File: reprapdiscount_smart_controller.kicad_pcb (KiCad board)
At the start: 2 copper layers, 150 x 55 mm, 56 parts, among them J1 USB_A, Q1 BC817, Q2 BC817, U1 74HC4050, U2 74HC4050, U3 Pico

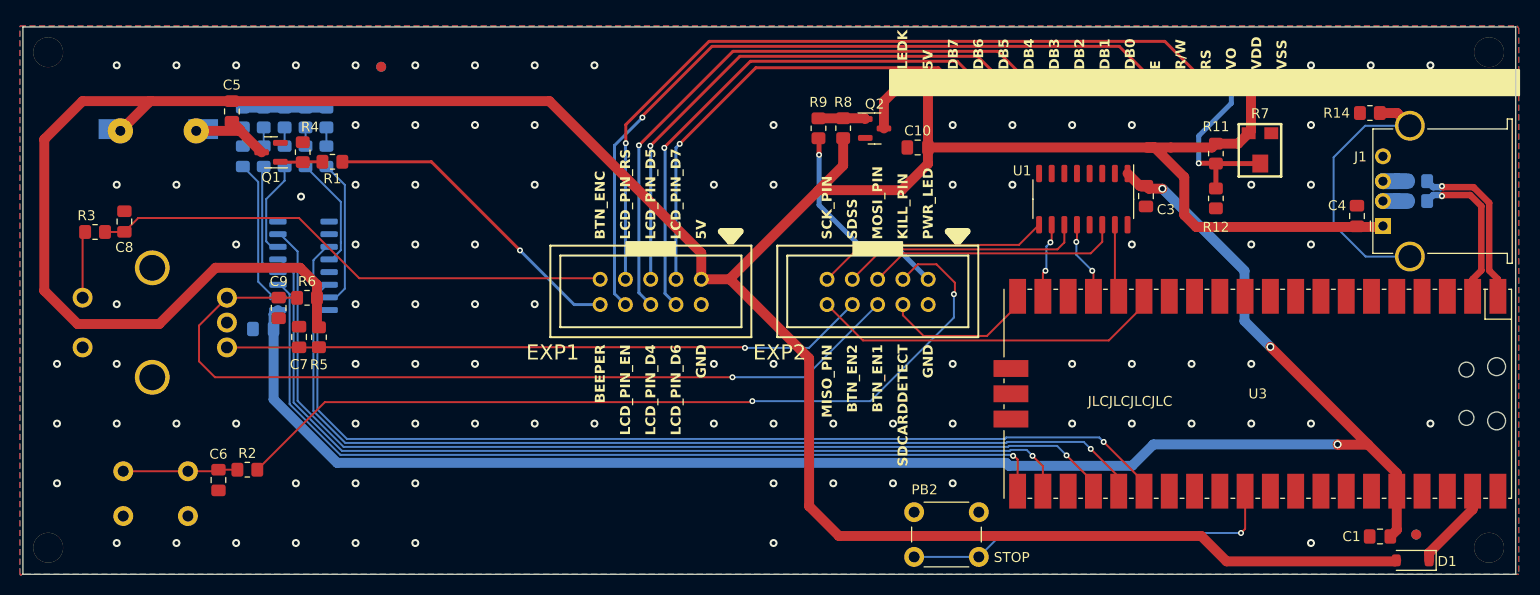
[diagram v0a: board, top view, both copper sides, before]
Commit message: feature: support adafruit rgb display
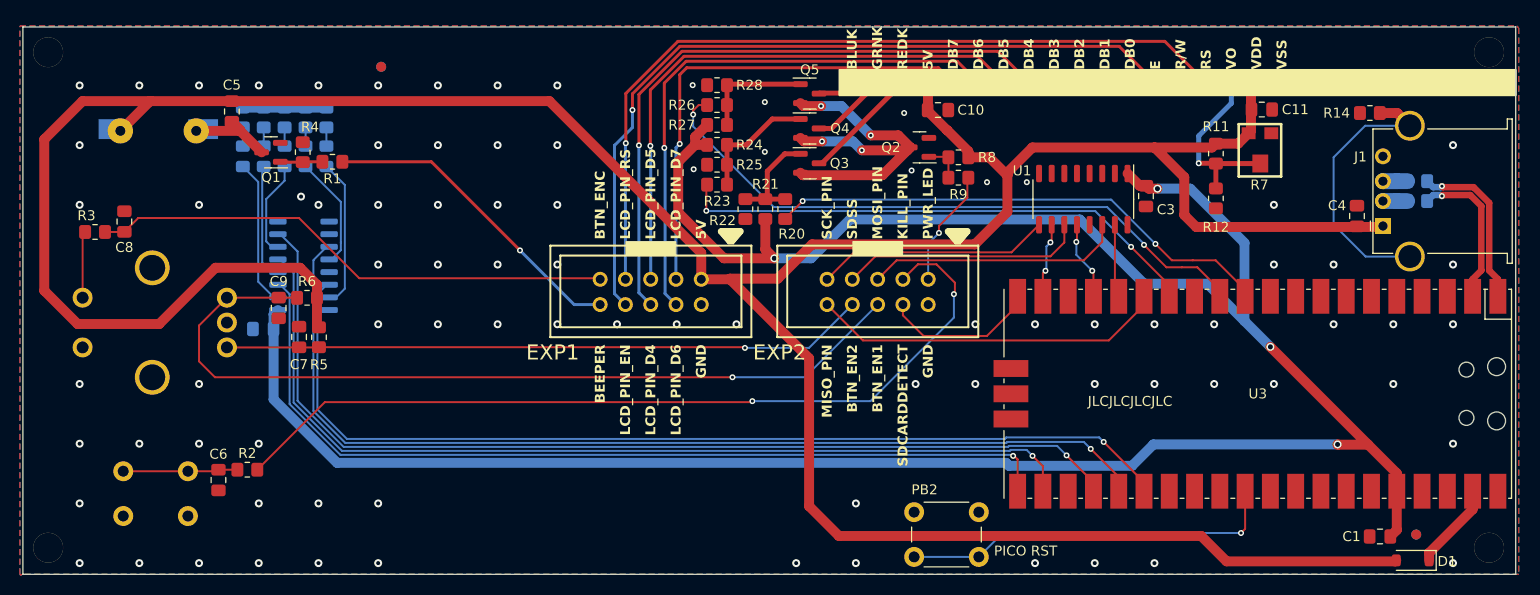
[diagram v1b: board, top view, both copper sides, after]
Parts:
- added C11: 10u, Capacitor_SMD:C_0805_2012Metric_Pad1.18x1.45mm_HandSolder, F.Cu at (198.0, 85.8)
- added Q3: DMN2005K-7, Package_TO_SOT_SMD:SOT-23, F.Cu at (152.6, 91.2)
- added Q4: DMN2005K-7, Package_TO_SOT_SMD:SOT-23, F.Cu at (152.6, 87.7)
- added Q5: DMN2005K-7, Package_TO_SOT_SMD:SOT-23, F.Cu at (152.6, 84.2)
- added R20: 0R, Resistor_SMD:R_0805_2012Metric_Pad1.20x1.40mm_HandSolder, F.Cu at (150.1, 95.8)
- added R21: 10k, Resistor_SMD:R_0805_2012Metric_Pad1.20x1.40mm_HandSolder, F.Cu at (148.1, 95.8)
- added R22: 10k, Resistor_SMD:R_0805_2012Metric_Pad1.20x1.40mm_HandSolder, F.Cu at (146.1, 95.8)
- added R23: 0R, Resistor_SMD:R_0805_2012Metric_Pad1.20x1.40mm_HandSolder, F.Cu at (143.2, 93.3)
- added R24: 10k, Resistor_SMD:R_0805_2012Metric_Pad1.20x1.40mm_HandSolder, F.Cu at (143.2, 89.3)
- added R25: 10k, Resistor_SMD:R_0805_2012Metric_Pad1.20x1.40mm_HandSolder, F.Cu at (143.2, 91.3)
- added R26: 0R, Resistor_SMD:R_0805_2012Metric_Pad1.20x1.40mm_HandSolder, F.Cu at (143.2, 85.3)
- added R27: 10k, Resistor_SMD:R_0805_2012Metric_Pad1.20x1.40mm_HandSolder, F.Cu at (143.2, 87.3)
- added R28: 10k, Resistor_SMD:R_0805_2012Metric_Pad1.20x1.40mm_HandSolder, F.Cu at (143.2, 83.3)
- LCD1: footprint reprapdiscount_smart_controller:HDR1X16 -> reprapdiscount_smart_controller:HDR1X18
- PB2: value STOP -> PICO RST
- Q1, Q2: value BC817 -> DMN2005K-7
- R1: value 1K -> 0R
- R15, R16, R18: value 1k -> 91R
- R17, R19: value 1k -> 33R
- R4: value 5.1k -> 0R
- R9: value 100R -> 0R
- moved R9 14.9 mm to (167.5, 92.7), turned to 0 degrees
- moved R8 11.9 mm to (167.5, 90.6), turned to 0 degrees
- moved Q2 4.90 mm to (163.6, 89.6), turned to 180 degrees
- moved C10 4.28 mm to (165.4, 85.8), turned to 180 degrees
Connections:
- LCD1 pad 16: LEDK -> REDK
- U3 pad 11: unconnected-(U3-GPIO8-Pad11) -> LEDR
- U3 pad 12: unconnected-(U3-GPIO9-Pad12) -> LEDB
- U3 pad 13: unconnected-(U3-GND-Pad13) -> GND
- U3 pad 14: unconnected-(U3-GPIO10-Pad14) -> LEDG
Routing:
- net +3V3: track 171.9 -> 253.9 mm, vias 3 -> 4
- net LEDB: track 0.00 -> 64.6 mm, vias 0 -> 2
- net LEDG: track 0.00 -> 54.3 mm, vias 0 -> 2
- net LEDR: track 0.00 -> 52.4 mm, vias 0 -> 2
- net LEDK: track 5.39 -> 36.9 mm, vias 0 -> 4
- net Net-(Q4-G): track 0.00 -> 12.5 mm
- net REDK: track 0.00 -> 11.8 mm
- net Net-(Q5-G): track 0.00 -> 11.4 mm
- net Net-(Q3-G): track 0.00 -> 10.9 mm
- net PWR_LED: track 20.8 -> 11.9 mm
- net GRNK: track 0.00 -> 7.77 mm
- net LCD7: track 45.0 -> 49.1 mm
- net BLUK: track 0.00 -> 3.78 mm
- net LCD6: track 52.3 -> 56.1 mm
- net LCD5: track 53.8 -> 57.0 mm
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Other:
- board text added: "BLUK"
- board text added: "GRNK"
- board text added: "REDK"
- board text removed: "LEDK"

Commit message: feature: add pico debug connections, testpoints
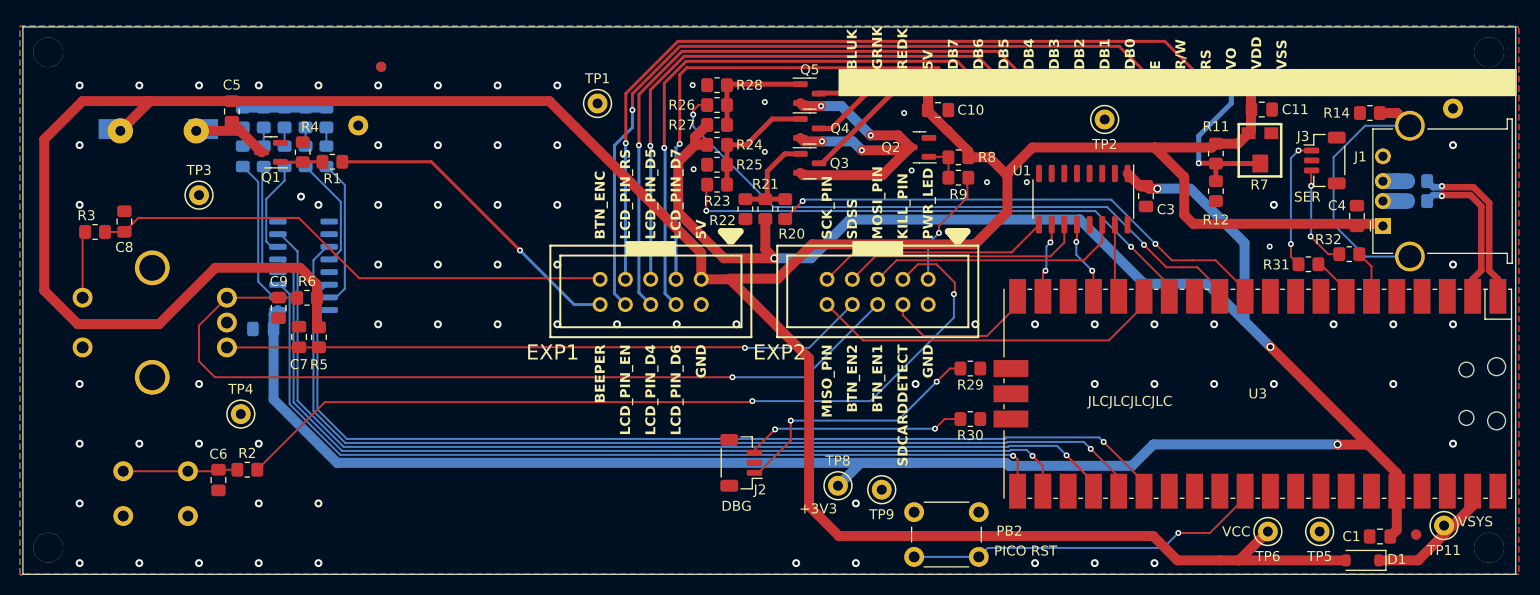
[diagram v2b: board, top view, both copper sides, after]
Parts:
- added J2: Conn_01x03_Pin, Gigahawk:JST_SH_BM03B-SRSS-TB_1x03-1MP_P1.00mm_Vertical, F.Cu at (145.7, 121.3)
- added J3: Conn_01x03_Pin, Gigahawk:JST_SH_BM03B-SRSS-TB_1x03-1MP_P1.00mm_Vertical, F.Cu at (204.3, 90.9)
- added R29: 100R, Resistor_SMD:R_0805_2012Metric_Pad1.20x1.40mm_HandSolder, F.Cu at (168.7, 111.8)
- added R30: 100R, Resistor_SMD:R_0805_2012Metric_Pad1.20x1.40mm_HandSolder, F.Cu at (168.7, 116.9)
- added R31: 100R, Resistor_SMD:R_0805_2012Metric_Pad1.20x1.40mm_HandSolder, F.Cu at (202.7, 101.3)
- added R32: 100R, Resistor_SMD:R_0805_2012Metric_Pad1.20x1.40mm_HandSolder, F.Cu at (206.8, 100.3)
- added TP1: TestPoint, Gigahawk:TestPoint_Keystone_5000-5004_Miniature, F.Cu at (131.2, 85.2)
- added TP10: TestPoint, Gigahawk:TestPoint_Keystone_5000-5004_Miniature, B.Cu at (217.2, 85.7)
- added TP11: TestPoint, Gigahawk:TestPoint_Keystone_5000-5004_Miniature, F.Cu at (216.3, 127.6)
- added TP2: TestPoint, Gigahawk:TestPoint_Keystone_5000-5004_Miniature, F.Cu at (182.2, 86.8)
- added TP3: TestPoint, Gigahawk:TestPoint_Keystone_5000-5004_Miniature, F.Cu at (91.2, 94.4)
- added TP4: TestPoint, Gigahawk:TestPoint_Keystone_5000-5004_Miniature, F.Cu at (95.4, 116.4)
- added TP5: TestPoint, Gigahawk:TestPoint_Keystone_5000-5004_Miniature, F.Cu at (203.8, 128.2)
- added TP6: TestPoint, Gigahawk:TestPoint_Keystone_5000-5004_Miniature, F.Cu at (198.6, 128.2)
- added TP7: TestPoint, Gigahawk:TestPoint_Keystone_5000-5004_Miniature, B.Cu at (107.2, 87.4)
- added TP8: TestPoint, Gigahawk:TestPoint_Keystone_5000-5004_Miniature, F.Cu at (155.4, 123.6)
- added TP9: TestPoint, Gigahawk:TestPoint_Keystone_5000-5004_Miniature, F.Cu at (159.8, 124.0)
- R14: value 0 -> 0R
- moved D1 5.05 mm to (208.1, 131.1)
- moved R12 0.73 mm to (193.4, 94.0)
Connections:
- net Net-(D1-K) renamed VSYS
- U3 pad 41: unconnected-(U3-SWCLK-Pad41) -> SWCLK
- U3 pad 43: unconnected-(U3-SWDIO-Pad43) -> SWDIO
- U3 pad 6: unconnected-(U3-GPIO4-Pad6) -> DBG_TX
- U3 pad 7: unconnected-(U3-GPIO5-Pad7) -> DBG_RX
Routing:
- net Net-(J2-Pin_1): track 0.00 -> 26.2 mm, vias 0 -> 2
- net Net-(J2-Pin_3): track 0.00 -> 22.3 mm, vias 0 -> 2
- net Net-(J3-Pin_1): track 0.00 -> 13.4 mm, vias 0 -> 2
- net Net-(J3-Pin_3): track 0.00 -> 10.3 mm, vias 0 -> 2
- net +3V3: track 253.9 -> 262.3 mm
- net VSYS: track 8.46 -> 14.9 mm
- net DBG_TX: track 0.00 -> 5.65 mm
- net DBG_RX: track 0.00 -> 5.42 mm
- net PICO_RST: track 37.9 -> 36.1 mm
- net unconnected-(U3-GPIO21-Pad27): track 0.00 -> 1.57 mm
- net VCC: track 331.0 -> 329.9 mm
- net Net-(LCD1-Vo): track 18.2 -> 17.4 mm
- net GND: vias 85 -> 79
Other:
- board text added: "+3V3"
- board text added: "DBG"
- board text added: "SER"
- board text added: "VCC"
- board text added: "VSYS"

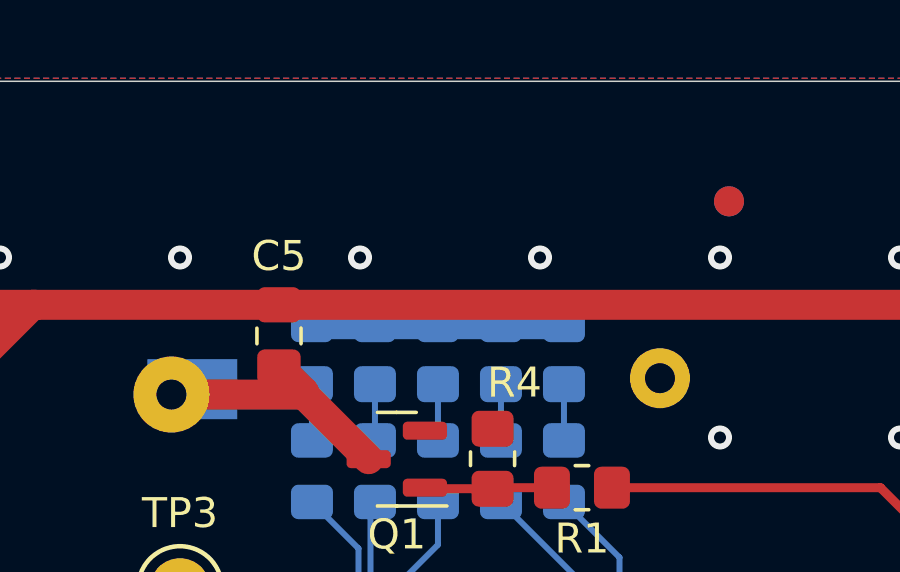
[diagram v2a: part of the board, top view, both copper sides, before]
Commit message: cleanup: remove vias blocking silkscreen
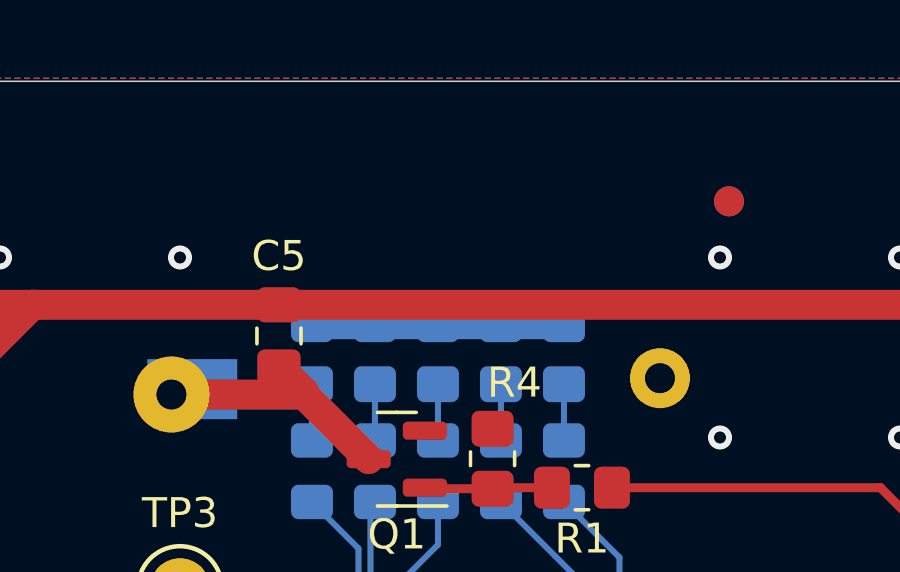
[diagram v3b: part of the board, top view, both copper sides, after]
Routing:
- net GND: vias 79 -> 77
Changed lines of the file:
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@@
   (via (at 115.2011 101.37661) (size 0.8) (drill 0.4) (layers "F.Cu" "B.Cu") (free) (net 6))
   (via (at 85.2011 131.37661) (size 0.8) (drill 0.4) (layers "F.Cu" "B.Cu") (free) (net 6))
-  (via (at 97.2011 83.37661) (size 0.8) (drill 0.4) (layers "F.Cu" "B.Cu") (free) (net 6))
   (via (at 198.7804 99.568) (size 0.6) (drill 0.3) (layers "F.Cu" "B.Cu") (free) (net 6))
   (via (at 162.8 91.925) (size 0.6) (drill 0.3) (layers "F.Cu" "B.Cu") (free) (net 6))
@@
   (via (at 101.45 94.55) (size 0.8) (drill 0.4) (layers "F.Cu" "B.Cu") (free) (net 6))
   (via (at 187.2011 113.37661) (size 0.8) (drill 0.4) (layers "F.Cu" "B.Cu") (free) (net 6))
-  (via (at 103.2011 83.37661) (size 0.8) (drill 0.4) (layers "F.Cu" "B.Cu") (free) (net 6))
   (via (at 181.2011 113.37661) (size 0.8) (drill 0.4) (layers "F.Cu" "B.Cu") (free) (net 6))
   (via (at 145.2011 107.37661) (size 0.8) (drill 0.4) (layers "F.Cu" "B.Cu") (free) (net 6))
@@
       4e8e256f-4981-4389-9b58-7f31a528e733
       522d03e8-6ab9-434e-8bfb-561113a885ee
-      548677cb-9fb2-4119-b621-b5bee12dc711
       5ad06bdc-7118-46ab-8166-f7b2b22e0552
       63902e67-80e1-4509-bfcc-47750150647f
@@
       b4cedc7c-fc88-4c58-a75a-b5b701a78534
       b8d70ceb-a417-4ead-9f93-bc9e32175272
-      beca6225-97a9-4a70-8827-ce1185b155ff
       c3c090b5-4498-44ca-82a3-3b4df6b2b2de
       c79265a8-7a71-44b9-841b-5fecbeb5646a

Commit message: all: add oshw logo to design
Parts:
- added SYM1: Logo_Open_Hardware_Large, Gigahawk:OSHW-Logo2_9.8x8mm_Mask, B.Cu at (103.2, 126.0)
